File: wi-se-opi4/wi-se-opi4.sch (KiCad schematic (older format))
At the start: 34 parts, among them J1 UART, J2 Side, Q1 SS8050-G, Q2 SS8050-G, SW1 RESET, SW2 BOOT0, U1 AMS1117-3.3, U2 ESP-WROOM-02

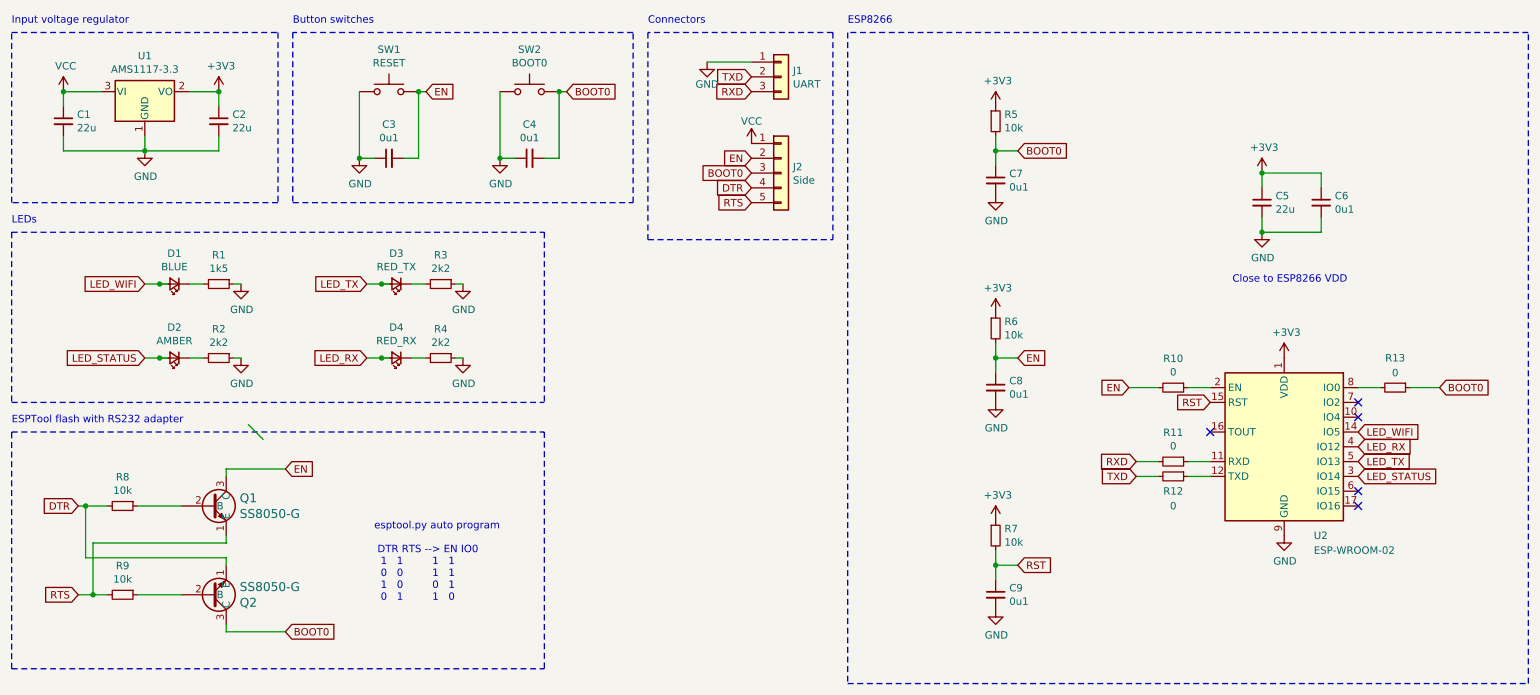
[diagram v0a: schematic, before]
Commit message: Update Opi4 version
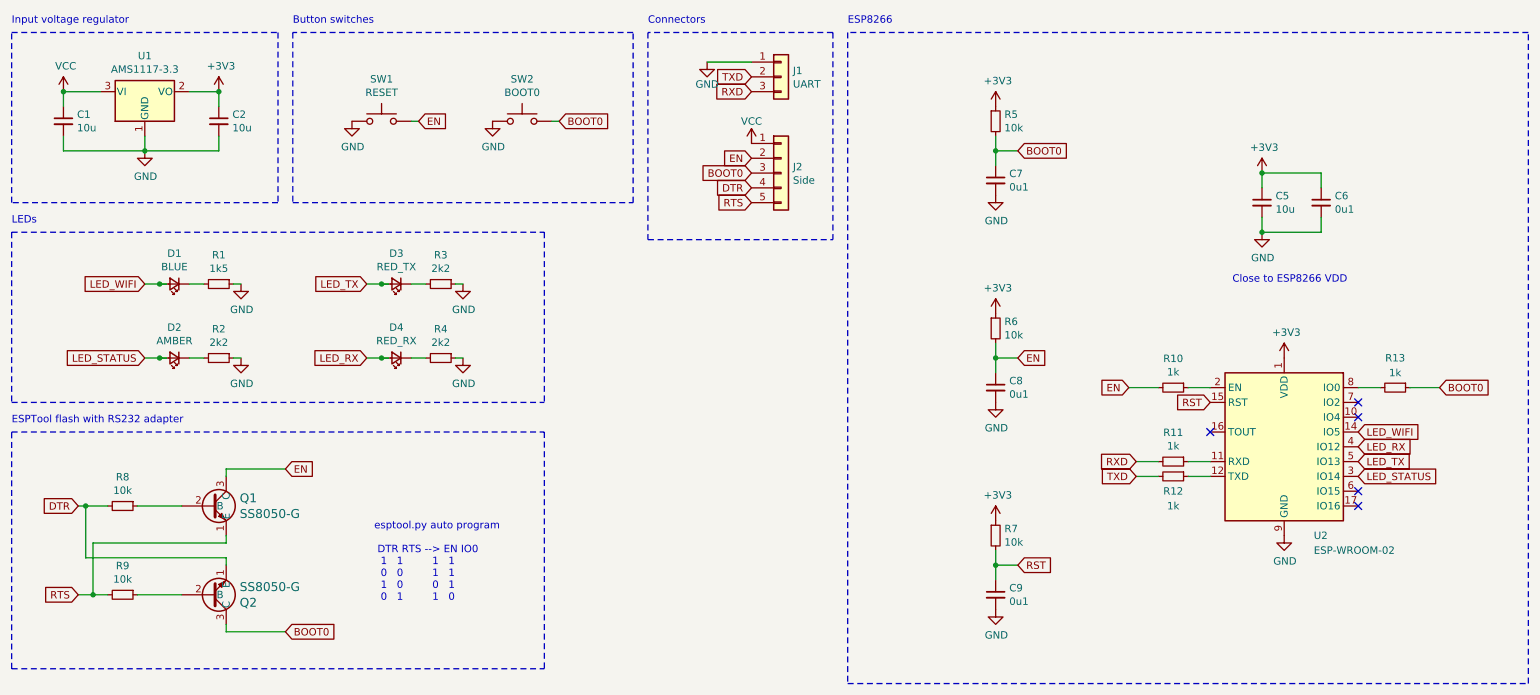
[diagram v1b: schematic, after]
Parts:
- removed C3, C4: 0u1, Capacitor_SMD:C_0603_1608Metric_Pad1.08x0.95mm_HandSolder, symbol Device:C_Small
- C1: value 22u -> 10u; LCSC Part (none) -> C13585
- C2, C5: value 22u -> 10u; footprint Capacitor_SMD:C_1206_3216Metric_Pad1.33x1.80mm_HandSolder -> Capacitor_SMD:C_1206_3216Metric; LCSC Part (none) -> C13585
- C6: footprint Capacitor_SMD:C_0603_1608Metric_Pad1.08x0.95mm_HandSolder -> Capacitor_SMD:C_0603_1608Metric; LCSC Part (none) -> C14663
- C7, C8, C9: footprint Capacitor_SMD:C_0603_1608Metric_Pad1.08x0.95mm_HandSolder -> Capacitor_SMD:C_0402_1005Metric; LCSC Part (none) -> C1546
- Q1, Q2: LCSC Part (none) -> C2150
- R1: footprint Resistor_SMD:R_0603_1608Metric_Pad0.98x0.95mm_HandSolder -> Resistor_SMD:R_0402_1005Metric; LCSC Part (none) -> C25867
- R10, R13: value 0 -> 1k; LCSC Part (none) -> C21190
- R11, R12: value 0 -> 1k; footprint Resistor_SMD:R_0603_1608Metric_Pad0.98x0.95mm_HandSolder -> Resistor_SMD:R_0402_1005Metric; LCSC Part (none) -> C25744
- R2, R3, R4: footprint Resistor_SMD:R_0603_1608Metric_Pad0.98x0.95mm_HandSolder -> Resistor_SMD:R_0402_1005Metric; LCSC Part (none) -> C25879
- R5, R6, R7, R8, R9: footprint Resistor_SMD:R_0603_1608Metric_Pad0.98x0.95mm_HandSolder -> Resistor_SMD:R_0402_1005Metric; LCSC Part (none) -> C25744
- U1: LCSC Part (none) -> C6186
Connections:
- wire segments 75 -> 67
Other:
- moved on the sheet: SW1, SW2

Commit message: Replace buttons with cheap aliexpress ones
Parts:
- SW1, SW2: footprint Button_Switch_SMD:SW_SPST_B3U-3100P -> aliexpress-switch:Tactile_Push_Button_SMD_3x3x1.5mm.kicad_mod
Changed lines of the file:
@@
 F 0 "SW1" H 3150 1635 50  0000 C CNN
 F 1 "RESET" H 3150 1544 50  0000 C CNN
-F 2 "Button_Switch_SMD:SW_SPST_B3U-3100P" H 3150 1550 50  0001 C CNN
+F 2 "aliexpress-switch:Tactile_Push_Button_SMD_3x3x1.5mm.kicad_mod" H 3150 1550 50  0001 C CNN
 F 3 "~" H 3150 1550 50  0001 C CNN
 	1    3150 1350
@@
 F 0 "SW2" H 4100 1635 50  0000 C CNN
 F 1 "BOOT0" H 4100 1544 50  0000 C CNN
-F 2 "Button_Switch_SMD:SW_SPST_B3U-3100P" H 4100 1550 50  0001 C CNN
+F 2 "aliexpress-switch:Tactile_Push_Button_SMD_3x3x1.5mm.kicad_mod" H 4100 1550 50  0001 C CNN
 F 3 "~" H 4100 1550 50  0001 C CNN
 	1    4100 1350

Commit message: opi4: Fix LCSC part number for UART resistors
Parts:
- R11, R12: LCSC Part C25744 -> C11702
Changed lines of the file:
@@
 F 2 "Resistor_SMD:R_0402_1005Metric" H 8500 3650 50  0001 C CNN
 F 3 "~" H 8500 3650 50  0001 C CNN
-F 4 "C25744" H 8500 3650 50  0001 C CNN "LCSC Part"
+F 4 "C11702" H 8500 3650 50  0001 C CNN "LCSC Part"
 	1    8500 3650
 	0    1    1    0
@@
 F 2 "Resistor_SMD:R_0402_1005Metric" H 8500 3750 50  0001 C CNN
 F 3 "~" H 8500 3750 50  0001 C CNN
-F 4 "C25744" H 8500 3750 50  0001 C CNN "LCSC Part"
+F 4 "C11702" H 8500 3750 50  0001 C CNN "LCSC Part"
 	1    8500 3750
 	0    1    1    0

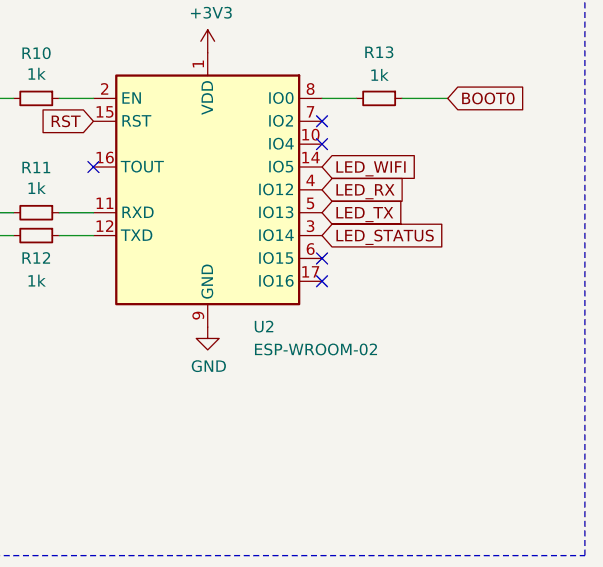
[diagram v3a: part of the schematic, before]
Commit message: opi4: Add missing GPIO15 pull-down
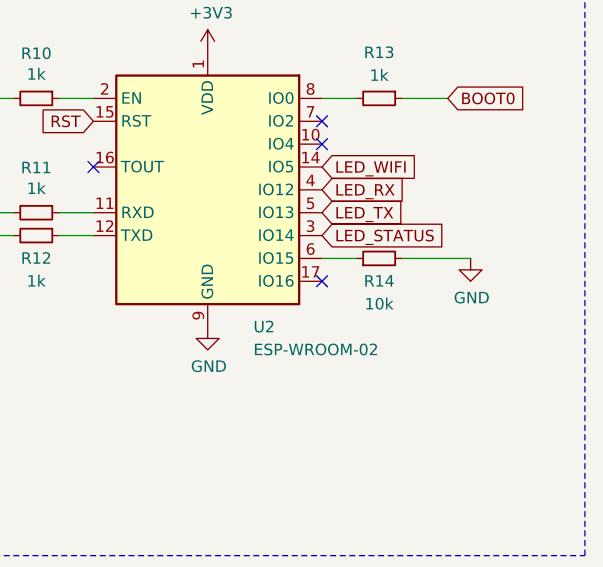
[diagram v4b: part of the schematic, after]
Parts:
- added R14: 10k, Resistor_SMD:R_0402_1005Metric, symbol Device:R_Small
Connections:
- wire segments 67 -> 69
- no-connect marks 5 -> 4
